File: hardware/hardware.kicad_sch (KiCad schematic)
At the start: 32 parts, among them J1 Conn_01x02, J2 Barrel_Jack, J3 USB_B_Micro, J4 Conn_01x02, J5 Conn_01x02, J6 Conn_01x02, Q1 BSS138, Q2 BSS138, U1 CH340C, U2 ESP32-WROOM-32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

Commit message: add ftdi
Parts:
- removed J2: Barrel_Jack, Connector_BarrelJack:BarrelJack_Wuerth_6941xx301002, symbol Connector:Barrel_Jack
- added J7: Conn_01x06, Connector_PinHeader_2.54mm:PinHeader_1x06_P2.54mm_Vertical, symbol Connector_Generic:Conn_01x06
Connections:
- net +BATT is gone; now on net +5V: C6.1, C7.1, C8.1, C9.1, U4.1 (VCC1), U4.4 (VDD1), U4.5 (VCC2), U4.8 (VDD2), U5.1 (VCC1), U5.4 (VDD1), U5.5 (VCC2), U5.8 (VDD2)
- net +5V: now also J7.4 (Pin_4)
- net GND: now also J7.6 (Pin_6)
- net RX-PROG: now also J7.2 (Pin_2)
- net TX-PROG: now also J7.3 (Pin_3)

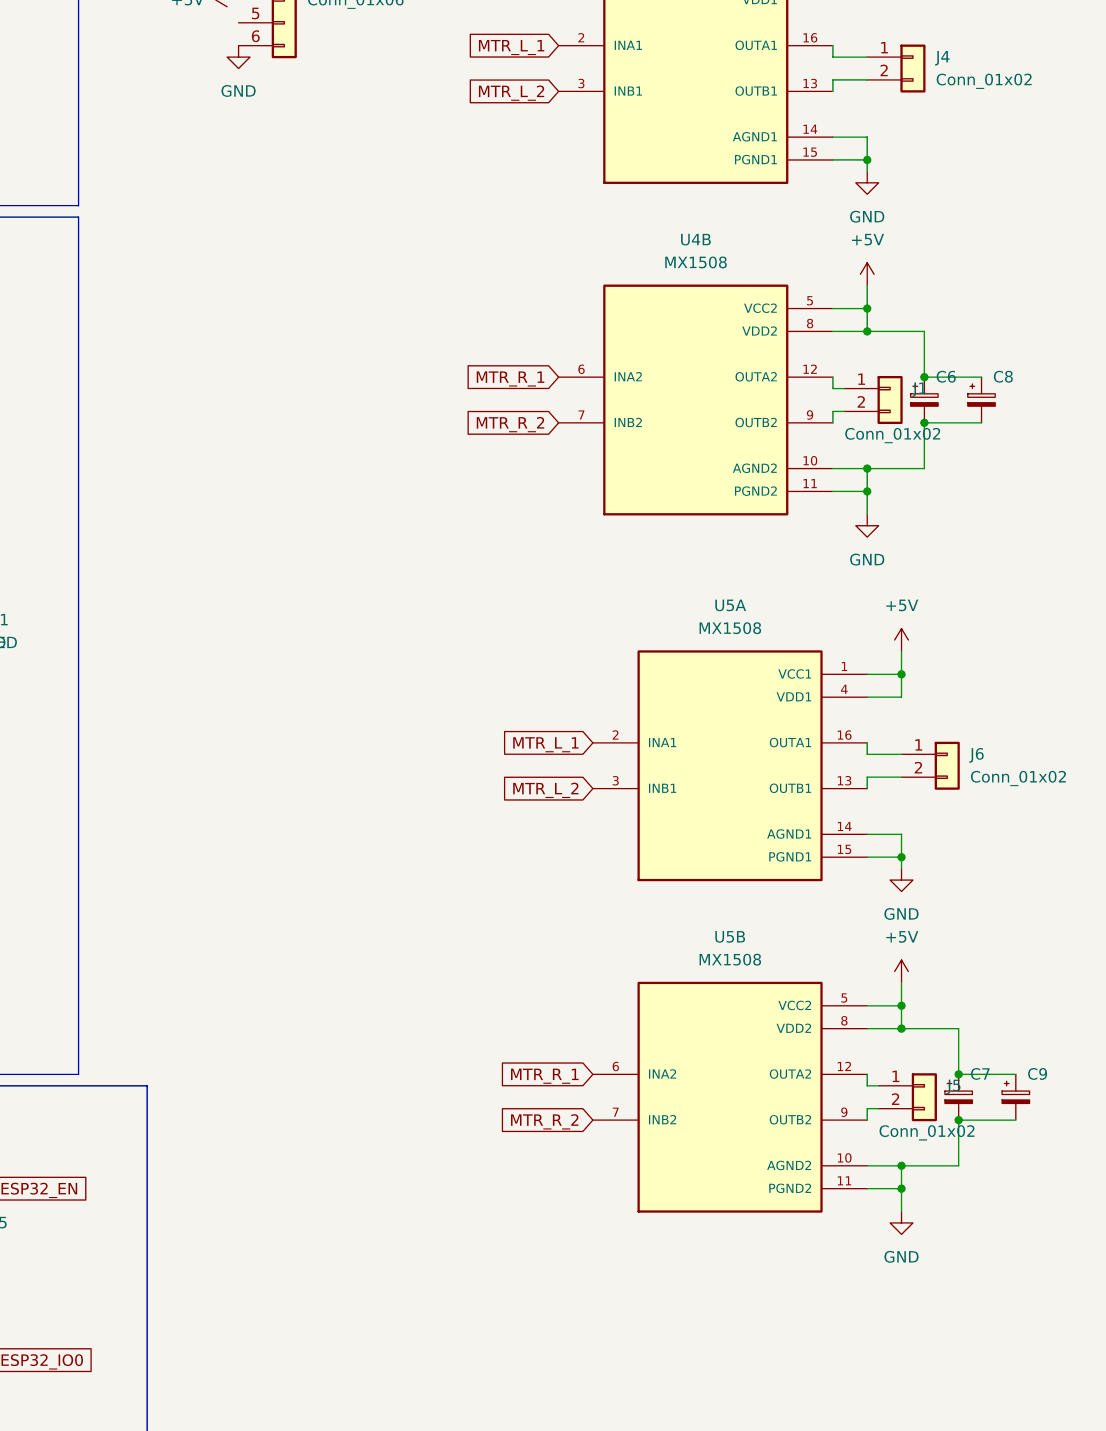
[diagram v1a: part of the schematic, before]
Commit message: place componants + mounting holes
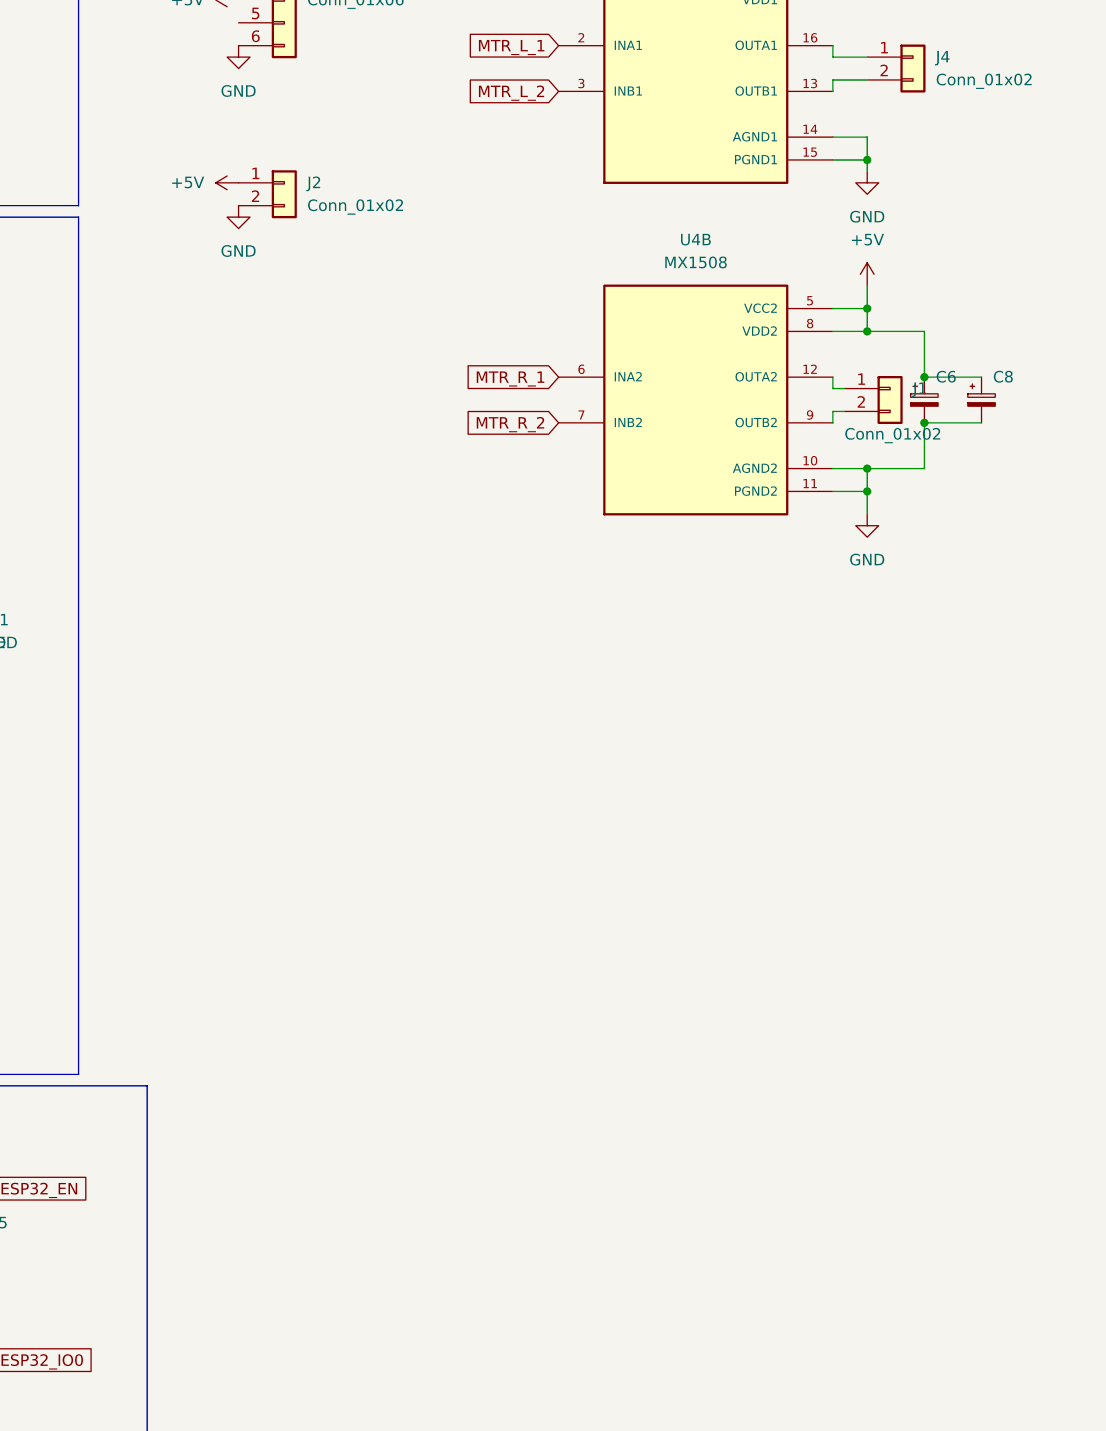
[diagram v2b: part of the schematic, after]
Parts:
- removed C7, C9: C_Polarized_Small, Capacitor_SMD:CP_Elec_6.3x4.9, symbol Device:C_Polarized_Small
- removed J5, J6: Conn_01x02, Connector_PinSocket_2.54mm:PinSocket_1x02_P2.54mm_Vertical, symbol Connector_Generic:Conn_01x02
- removed U5: MX1508, Package_SO:SOIC-16_3.9x9.9mm_P1.27mm, symbol MX1508:MX1508
- added J2: Conn_01x02, Connector_PinSocket_2.54mm:PinSocket_1x02_P2.54mm_Vertical, symbol Connector_Generic:Conn_01x02
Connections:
- net +5V: now also J2.1 (Pin_1)
- net GND: now also J2.2 (Pin_2)

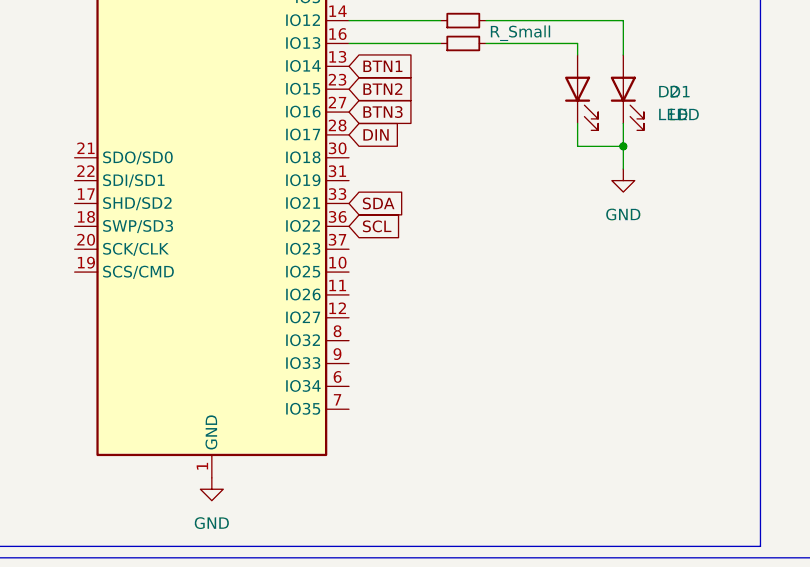
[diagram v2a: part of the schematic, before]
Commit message: add wiring mx1508 + vcc headers connector
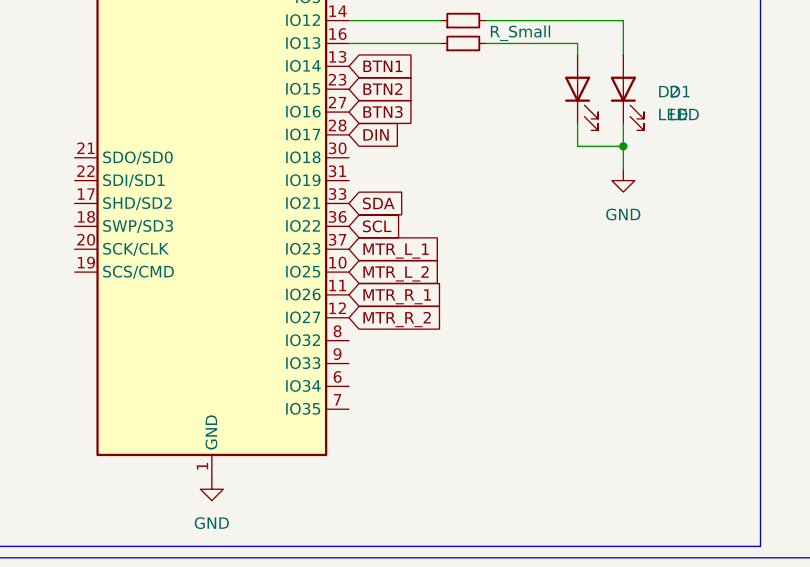
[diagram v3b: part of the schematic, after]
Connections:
- net MTR_L_1: now also U2.37 (IO23)
- net MTR_L_2: now also U2.10 (IO25)
- net MTR_R_1: now also U2.11 (IO26)
- net MTR_R_2: now also U2.12 (IO27)
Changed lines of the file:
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@@
+		)
+	)
+	(global_label "MTR_R_2"
+		(shape input)
+		(at 101.6 119.38 0)
+		(fields_autoplaced yes)
+		(effects
+			(font
+				(size 1.27 1.27)
+			)
+			(justify left)
+		)
+		(property "Intersheetrefs" "${INTERSHEET_REFS}"
+			(at 112.6889 119.38 0)
+			(effects
+				(font
+					(size 1.27 1.27)
+				)
+				(justify left)
+				(hide yes)
+			)
 		)
 	)
@@
 		)
 	)
+	(global_label "MTR_L_2"
+		(shape input)
+		(at 101.6 114.3 0)
+		(fields_autoplaced yes)
+		(effects
+			(font
+				(size 1.27 1.27)
+			)
+			(justify left)
+		)
+		(property "Intersheetrefs" "${INTERSHEET_REFS}"
+			(at 112.447 114.3 0)
+			(effects
+				(font
+					(size 1.27 1.27)
+				)
+				(justify left)
+				(hide yes)
+			)
+		)
+	)
 	(global_label "D+"
 		(shape input)
@@
 		)
 	)
+	(global_label "MTR_R_1"
+		(shape input)
+		(at 101.6 116.84 0)
+		(fields_autoplaced yes)
+		(effects
+			(font
+				(size 1.27 1.27)
+			)
+			(justify left)
+		)
+		(property "Intersheetrefs" "${INTERSHEET_REFS}"
+			(at 112.6889 116.84 0)
+			(effects
+				(font
+					(size 1.27 1.27)
+				)
+				(justify left)
+				(hide yes)
+			)
+		)
+	)
 	(global_label "ESP32_EN"
 		(shape input)
@@
 				(hide yes)
 			)
+		)
+	)
+	(global_label "MTR_L_1"
+		(shape input)
+		(at 101.6 111.76 0)
+		(fields_autoplaced yes)
+		(effects
+			(font
+				(size 1.27 1.27)
+			)
+			(justify left)
+		)
+		(property "Intersheetrefs" "${INTERSHEET_REFS}"
+			(at 112.447 111.76 0)
+			(effects
+				(font
+					(size 1.27 1.27)
+				)
+				(justify left)
+				(hide yes)
+			)
